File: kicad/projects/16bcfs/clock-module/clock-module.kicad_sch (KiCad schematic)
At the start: 38 parts, among them J1 Signals, J2 Power, J3 Power, J4 Power, SW1 Run, SW2 Single Step, SW3 SW_SPDT, U1 NE555D, U2 NE555D, U3 74HC00, U4 74HC08, U5 74HC32, U6 74HC74

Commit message: Add Register Module and update the Clock Module (#23)
* Completes #13
* Fixes #12
* Completes #14
* Completes #10
* Completes #18
* Fixes #22

Co-authored-by: Adam Clark <adam@eryjus.com>
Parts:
- removed U5: 74HC32, symbol eryjus:74HC32
- added U4: 74HC02, symbol 74xx:74HC02
- renumbered C4 to C3, C3 to C4, R2 to R1, R3 to R2, R1 to R3, R9 to R4, R8 to R5, R4 to R6, R5 to R7, R6 to R8, R7 to R9, SW3 to SW1, SW1 to SW2, SW2 to SW3, U3 to U1, U1 to U3, U6 to U5, U4 to U6
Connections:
- net CLK: now also U4.1
- net GNDREF: now also U4.11, U4.12, U4.5, U4.6, U4.7 (GND), U4.8, U4.9; no longer R6.2
- net Oscillator: now also D1.1 (K); no longer D1.2 (A)
- net VCC: now also R6.2, U4.14 (VCC)
- net at U6.3: now also U4.2
- net at U6.6: now also U4.3
- net at R6.1: now also D1.2 (A); no longer D1.1 (K)
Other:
- note added: "Basic Oscillator"
- note added: "Final Clock Signal"
- note added: "Run Mode"
- note added: "Step Mode"
- moved on the sheet: D1, D2, D3, R6, R7, R8

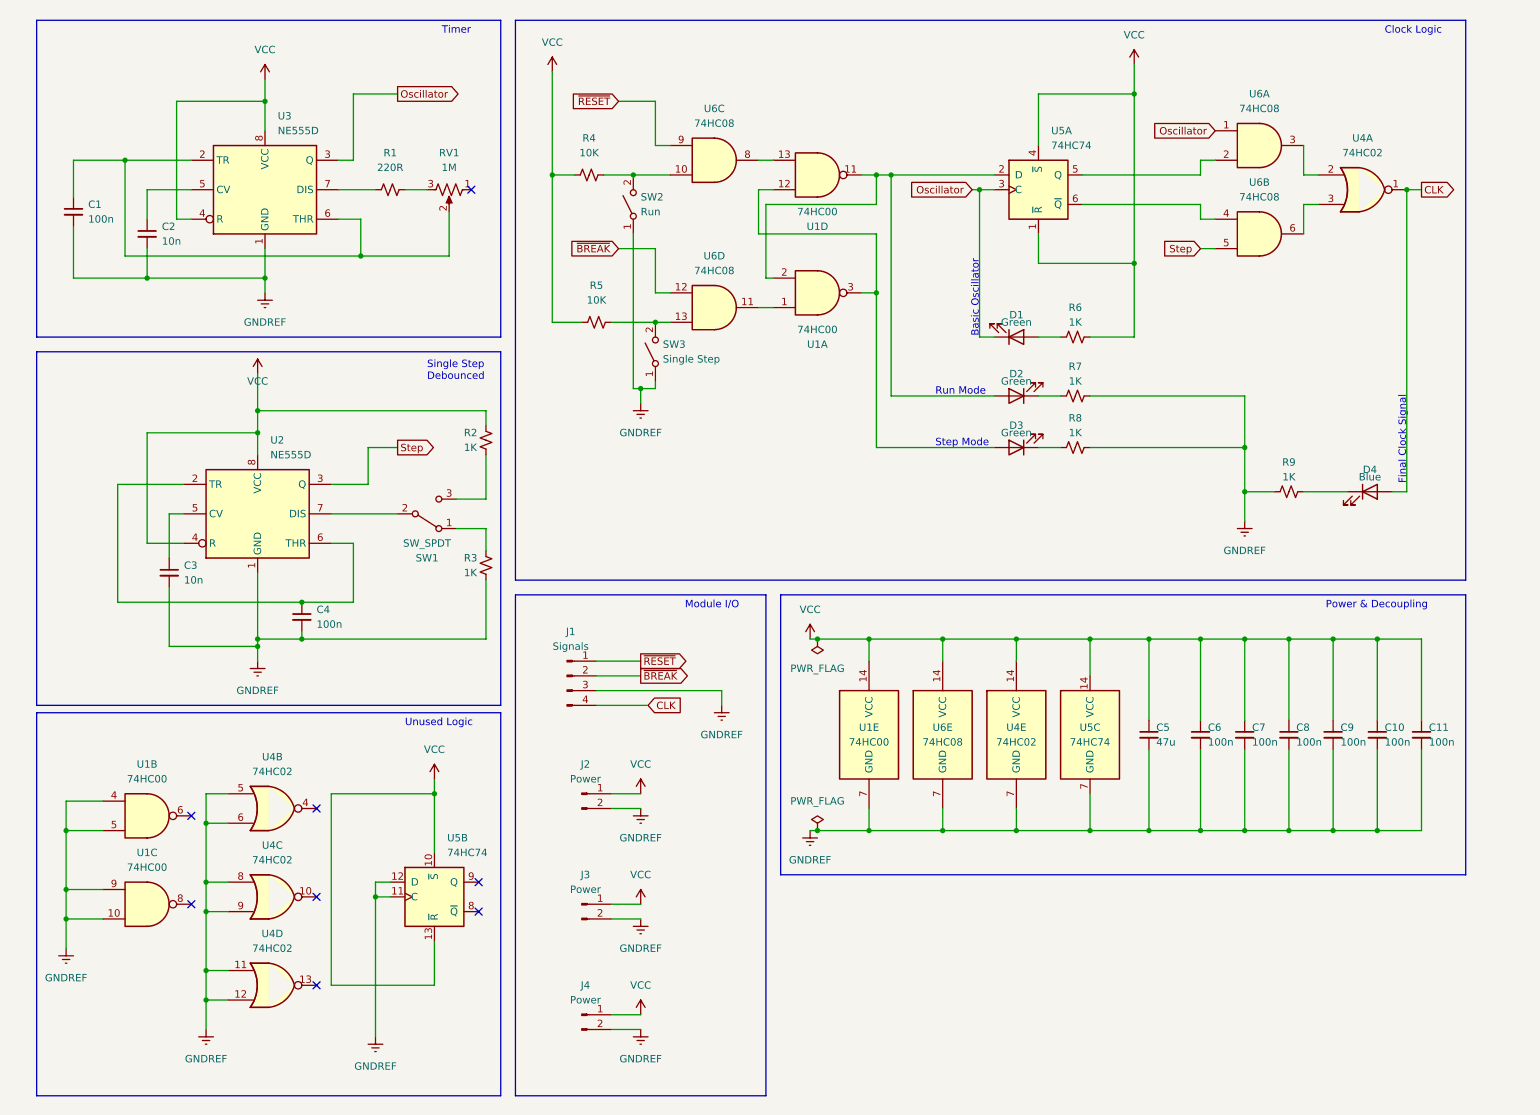
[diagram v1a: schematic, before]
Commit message: Create the Register Module Schematic (#37)
Co-authored-by: Adam Clark <adam@eryjus.com>
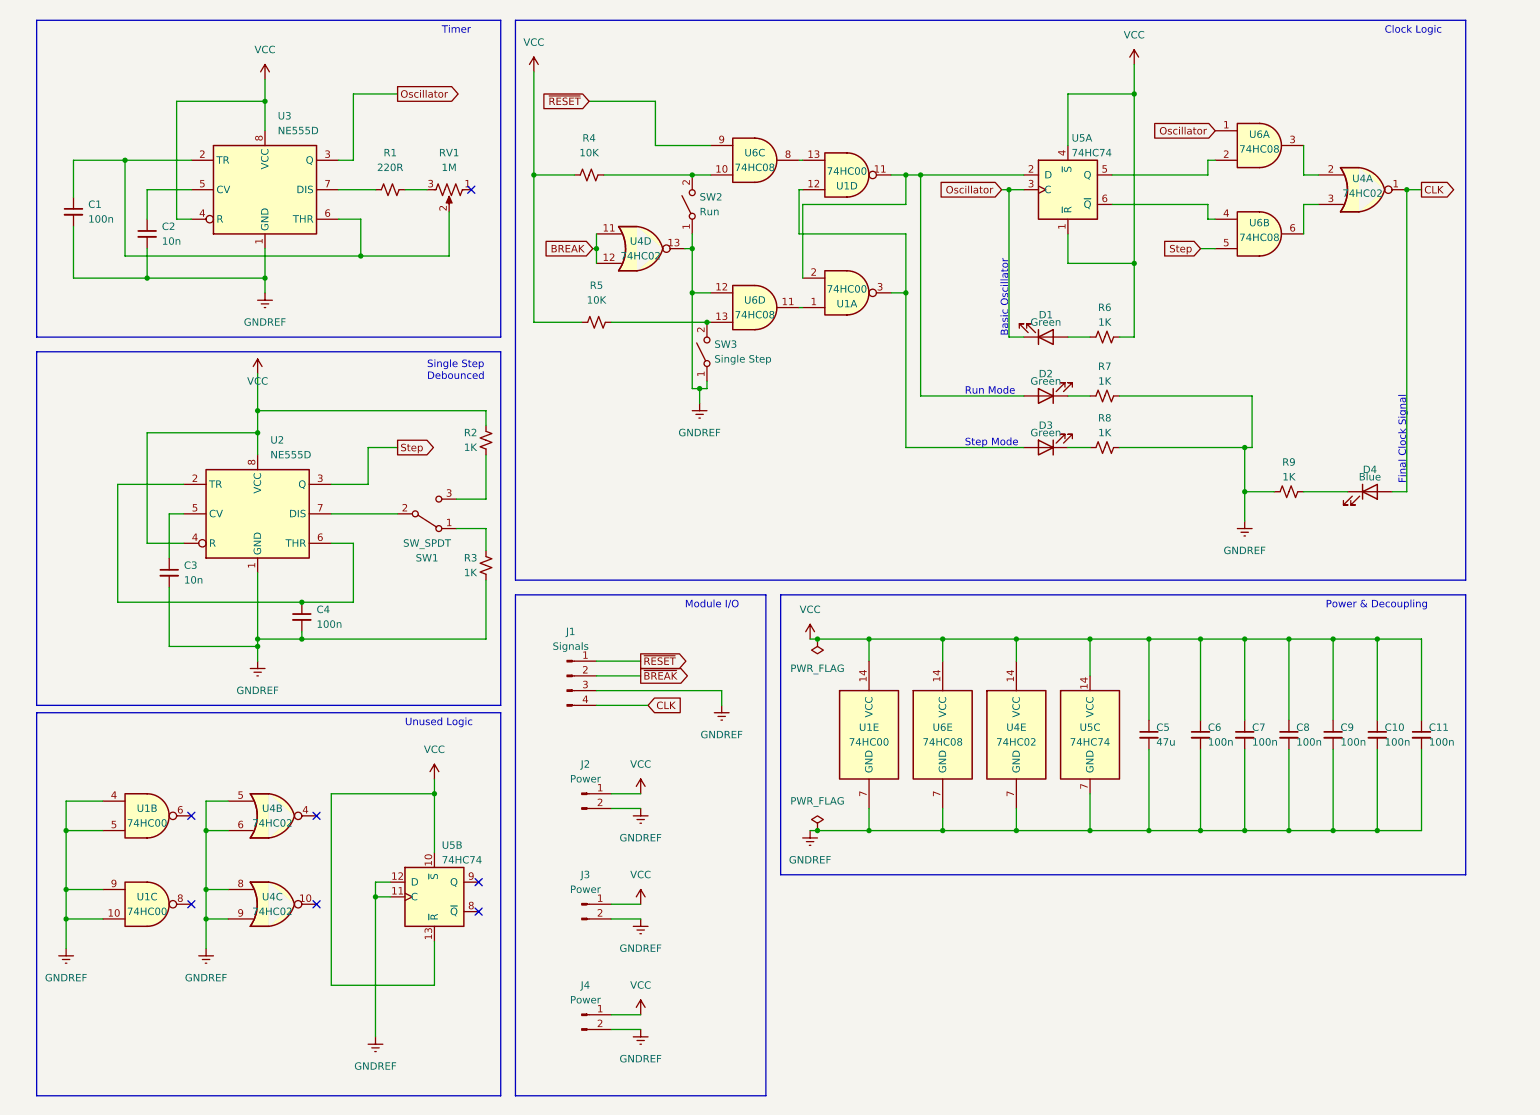
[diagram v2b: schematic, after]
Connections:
- net GNDREF: now also U4.13, U6.12; no longer U4.11, U4.12
- net ~{BREAK}: no longer U6.12
- new net BREAK: U4.11, U4.12
- no-connect marks 8 -> 7
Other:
- moved on the sheet: D1, D2, D3, R6, R7, R8, SW2, SW3, U1A, U1D, U4B, U4C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

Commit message: Update the Clock Module schematics
This is what I hope will be the final incarnation of the clock module,
making it all the way to the final build.
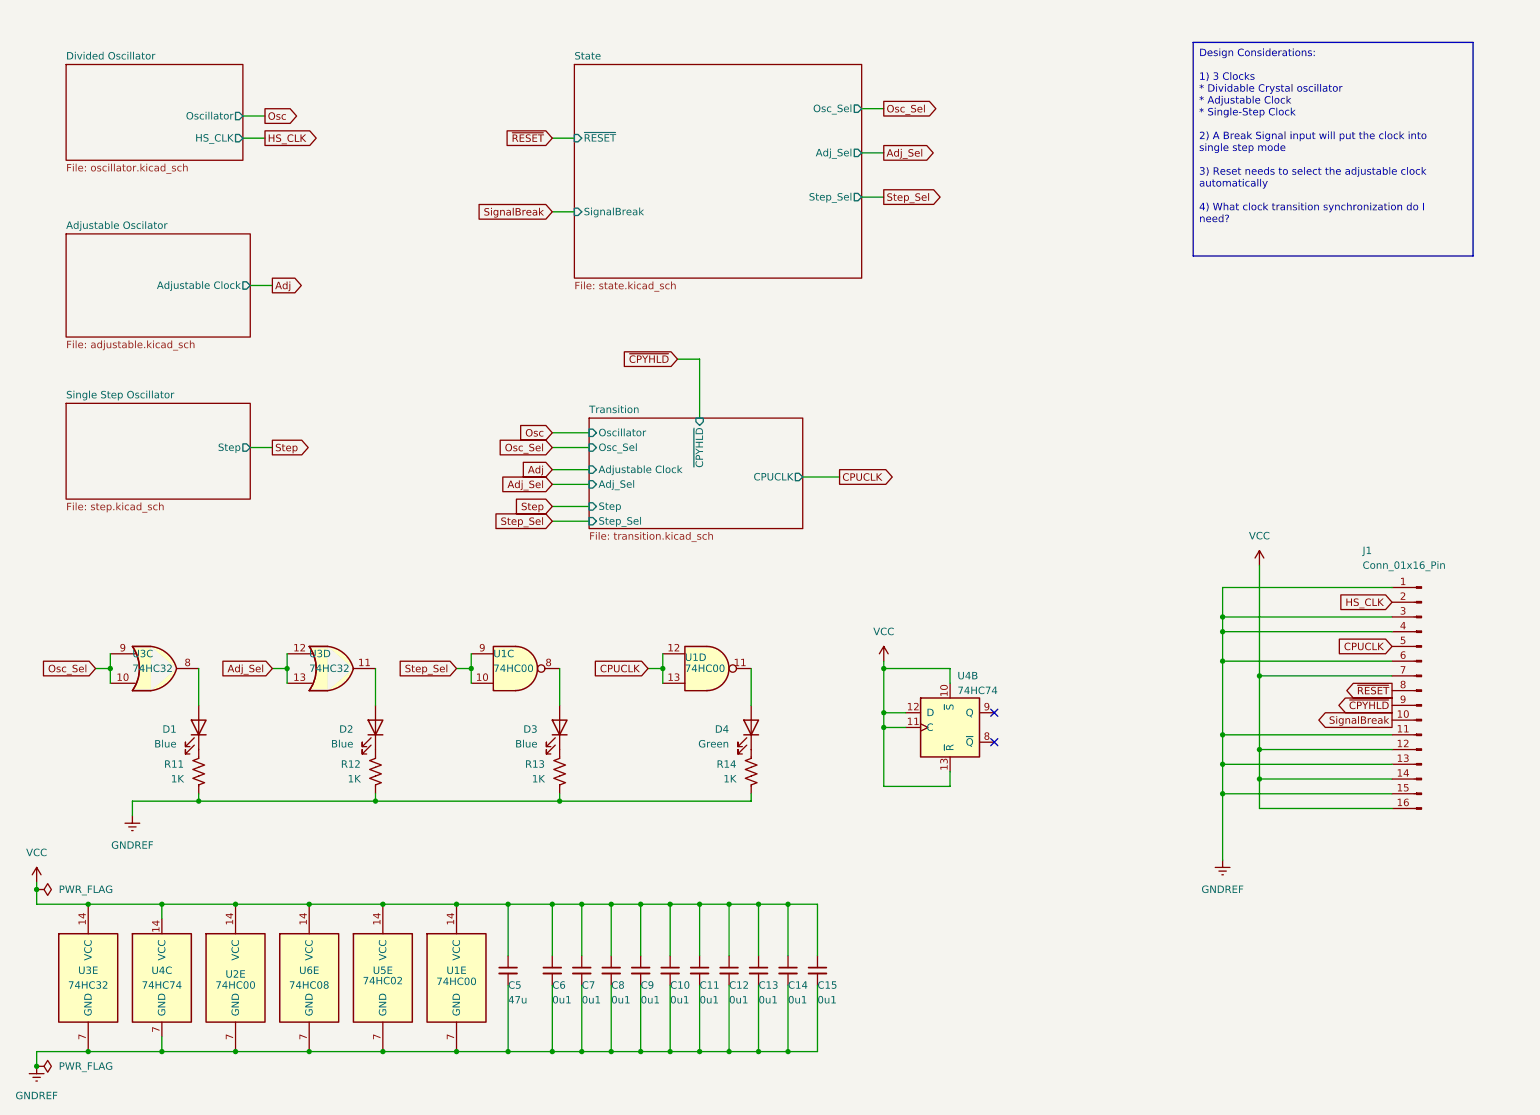
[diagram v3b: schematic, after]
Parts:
- removed C1, C4: 100n, symbol Device:C_Small
- removed C2, C3: 10n, symbol Device:C_Small
- removed J1: Signals, symbol Connector:Conn_01x04_Pin
- removed J2, J3, J4: Power, symbol Connector:Conn_01x02_Pin
- removed R1: 220R, symbol Device:R_Small_US
- removed R2, R3, R6, R7, R8, R9: 1K, symbol Device:R_Small_US
- removed R4, R5: 10K, symbol Device:R_Small_US
- removed RV1: 1M, symbol Device:R_Potentiometer_US
- removed SW1: SW_SPDT, symbol Switch:SW_SPDT
- removed SW2: Run, symbol Switch:SW_SPST
- removed SW3: Single Step, symbol Switch:SW_SPST
- removed unit 1 of U1
- removed unit 2 of U1
- removed U2, U3: NE555D, Package_SO:SOIC-8_3.9x4.9mm_P1.27mm, symbol Timer:NE555D
- removed U4: 74HC02, symbol 74xx:74HC02
- removed U5: 74HC74, symbol 74xx:74HC74
- removed unit 1 of U6
- removed unit 2 of U6
- removed unit 3 of U6
- removed unit 4 of U6
- added C12, C13, C14, C15: 0u1, symbol Device:C_Small
- added J1: Conn_01x16_Pin, symbol Connector:Conn_01x16_Pin
- added R11, R12, R13, R14: 1K, symbol Device:R_US
- added U2: 74HC00, symbol 74xx:74HC00
- added U3: 74HC32, symbol eryjus:74HC32
- added U4: 74HC74, symbol 74xx:74HC74
- added U5: 74HC02, symbol 74xx:74HC02
- C10, C11, C6, C7, C8, C9: value 100n -> 0u1
- D1, D2, D3: value Green -> Blue
- D4: value Blue -> Green
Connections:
- net CLK is gone; now on an unnamed net: D4.2 (A)
- net GNDREF: now also C12.2, C13.2, C14.2, C15.2, J1.1 (Pin_1), J1.11 (Pin_11), J1.13 (Pin_13), J1.15 (Pin_15), J1.3 (Pin_3), J1.4 (Pin_4), J1.6 (Pin_6), R11.2, R12.2, R13.2, R14.2, U2.7 (GND), U3.7 (GND), U4.7 (GND), U5.7 (GND); no longer U1.10, U1.9
- net VCC: now also C12.1, C13.1, C14.1, C15.1, J1.12 (Pin_12), J1.14 (Pin_14), J1.16 (Pin_16), J1.7 (Pin_7), U2.14 (VCC), U3.14 (VCC), U4.10 (~{S}), U4.11 (C), U4.12 (D), U4.13 (~{R}), U4.14 (VCC), U5.14 (VCC)
- net ~{RESET}: now also J1.8 (Pin_8)
- net at U1.11: no longer D2.2 (A)
- net at D3.2 (A): now also U1.8; no longer U1.12
- net CPUCLK: now reaches U1.13
- net CPUCLK: now also U1.12, J1.5 (Pin_5)
- net at D1.2 (A): now also U3.8
- net at D3.1 (K): now also R13.1
- net at D2.1 (K): now also R12.1
- net at D4.1 (K): now also R14.1
- net Oscillator: no longer names the net of D1.1 (K)
- net Oscillator: now also R11.1
- new net: D2.2 (A), U3.11
- new net Adj_Sel: U3.12, U3.13
- new net HS_CLK: J1.2 (Pin_2)
- new net Osc_Sel: U3.10, U3.9
- new net SignalBreak: J1.10 (Pin_10)
- new net Step_Sel: U1.10, U1.9
- new net ~{CPYHLD}: J1.9 (Pin_9)
- no-connect marks 7 -> 2
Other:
- added sheet Adjustable Oscilator (adjustable.kicad_sch)
- added sheet Divided Oscillator (oscillator.kicad_sch)
- added sheet Single Step Oscillator (step.kicad_sch)
- added sheet State (state.kicad_sch)
- added sheet Transition (transition.kicad_sch)
- note removed: "Basic Oscillator"
- note removed: "Clock Logic"
- note removed: "Final Clock Signal"
- note removed: "Module I/O"
- note removed: "Power & Decoupling"
- note removed: "Run Mode"
- note removed: "Single Step Debounced"
- note removed: "Step Mode"
- note removed: "Timer"
- note removed: "Unused Logic"

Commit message: Clean up the Reset and Clock Modules
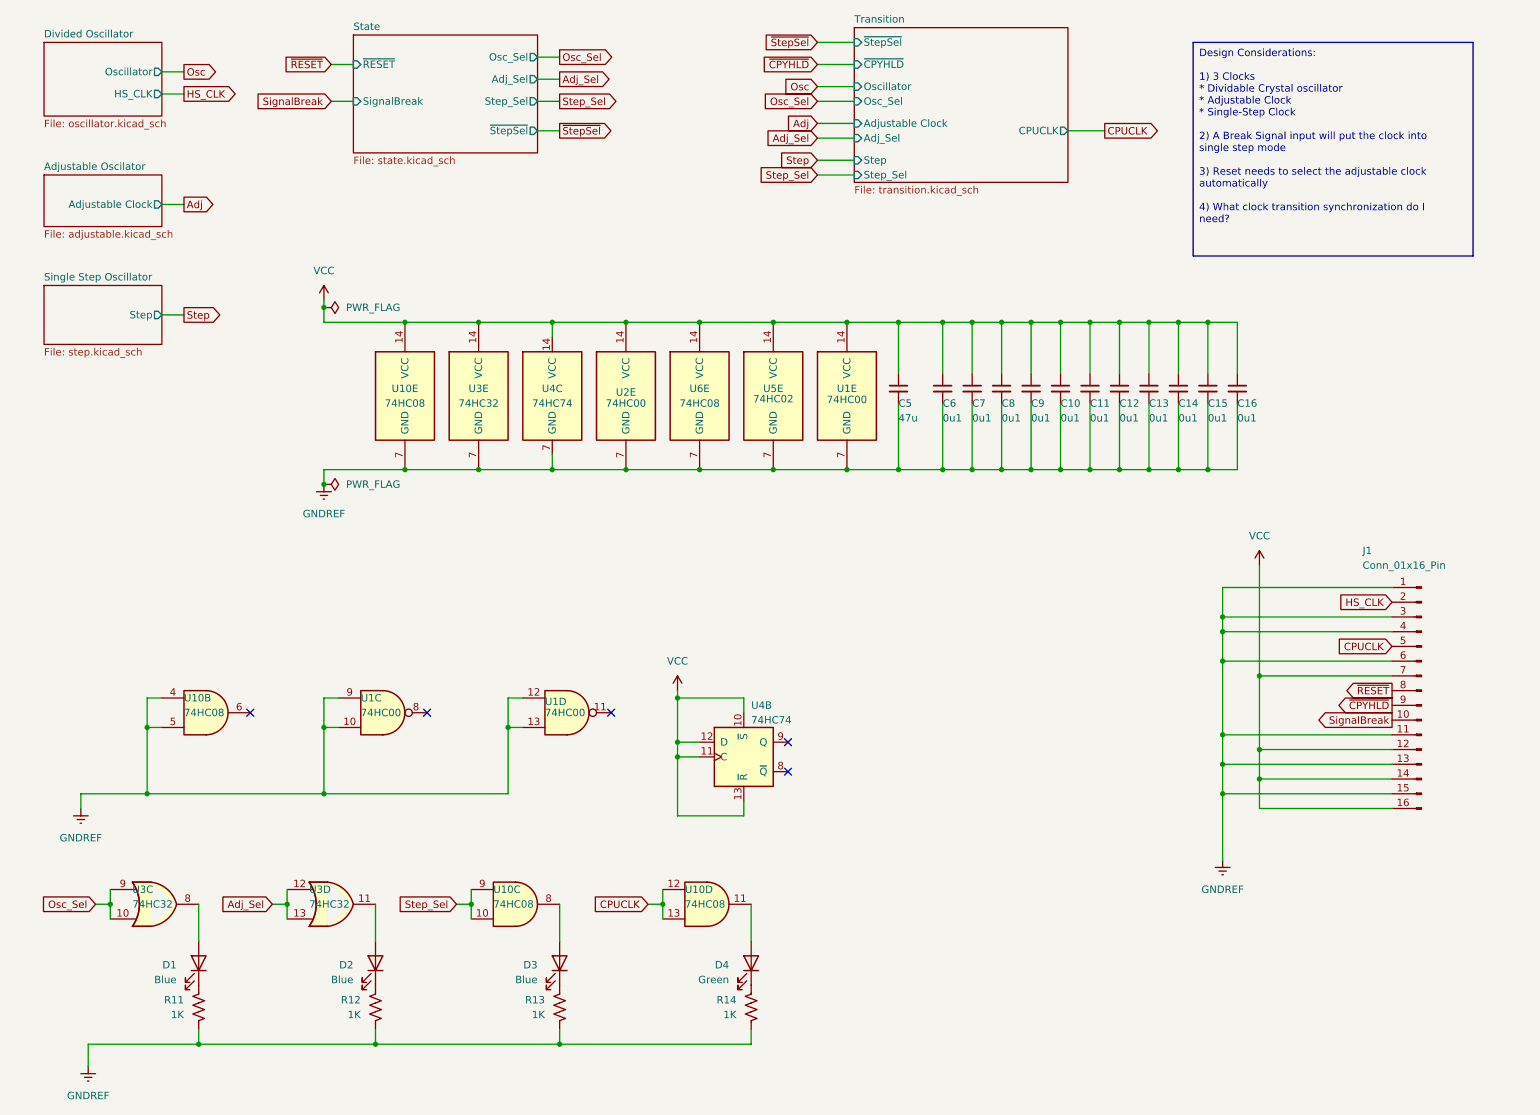
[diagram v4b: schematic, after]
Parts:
- added C16: 0u1, symbol Device:C_Small
- added U10: 74HC08, symbol eryjus:74HC08
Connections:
- net CPUCLK: now also U10.12, U10.13; no longer U1.12, U1.13
- net GNDREF: now also U1.10, U1.12, U1.13, U1.9, C16.2, U10.4, U10.5, U10.7 (GND)
- net Step_Sel: now also U10.10, U10.9; no longer U1.10, U1.9
- net VCC: now also C16.1, U10.14 (VCC)
- net at D3.2 (A): now also U10.8; no longer U1.8
- net at U1.11: no longer D4.2 (A)
- new net: D4.2 (A), U10.11
- no-connect marks 2 -> 5
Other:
- sheet State ports: added ~{StepSel}; removed none
- sheet Transition ports: added ~{StepSel}; removed none
- moved on the sheet: C10, C11, C12, C13, C14, C15, C5, C6, C7, C8, C9, D1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
